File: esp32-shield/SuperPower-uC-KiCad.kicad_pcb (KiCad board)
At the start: 2 copper layers, 45.1 x 45.1 mm, 33 parts, among them J11 DNP, J5 Conn_01x14_Female, J6 Conn_01x14_Female, J9 MCU board, Q3 S8050, Q4 S8050, U13 ESP32-WROOM32, U14 W25Q32JVSS, U5 CH340C, U6 AMS1117-3.3, Y1 12MHZ

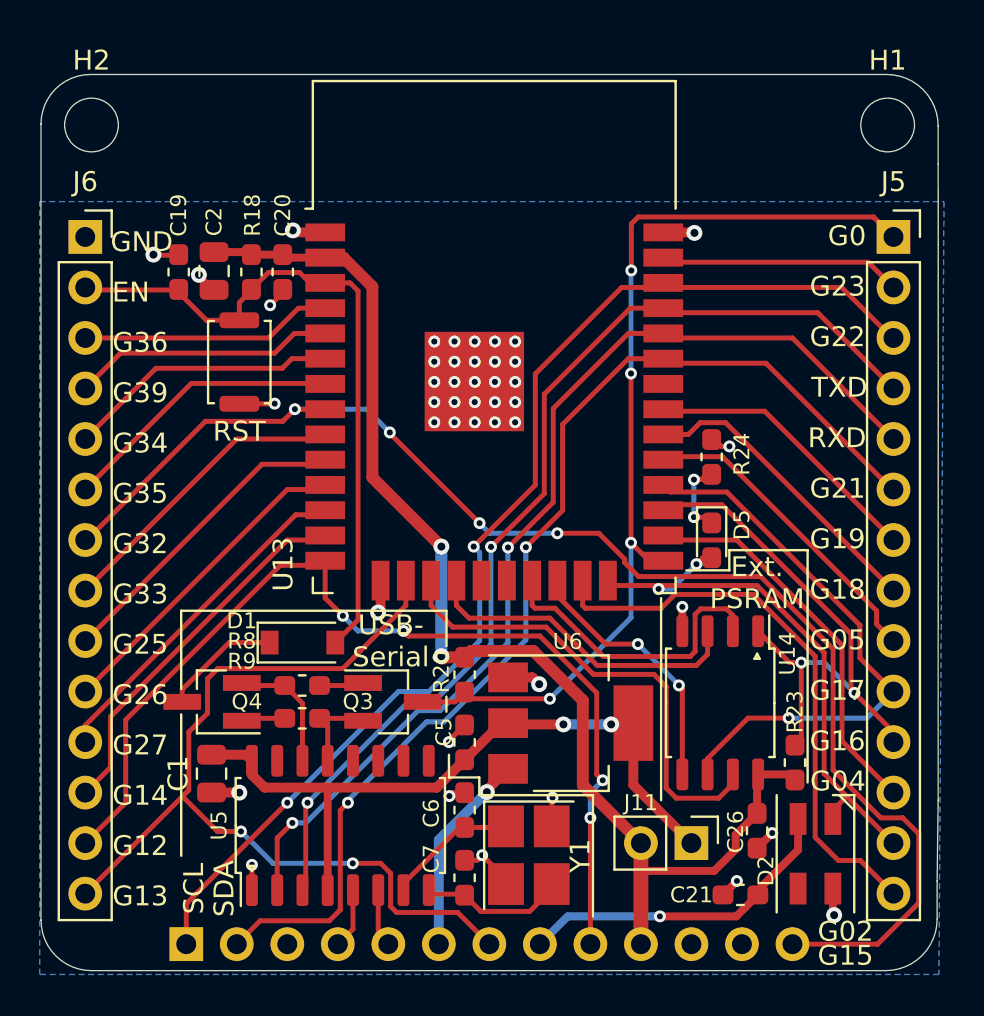
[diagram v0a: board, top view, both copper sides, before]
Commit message: swapped led for WS2812 footprint with logic level shifter
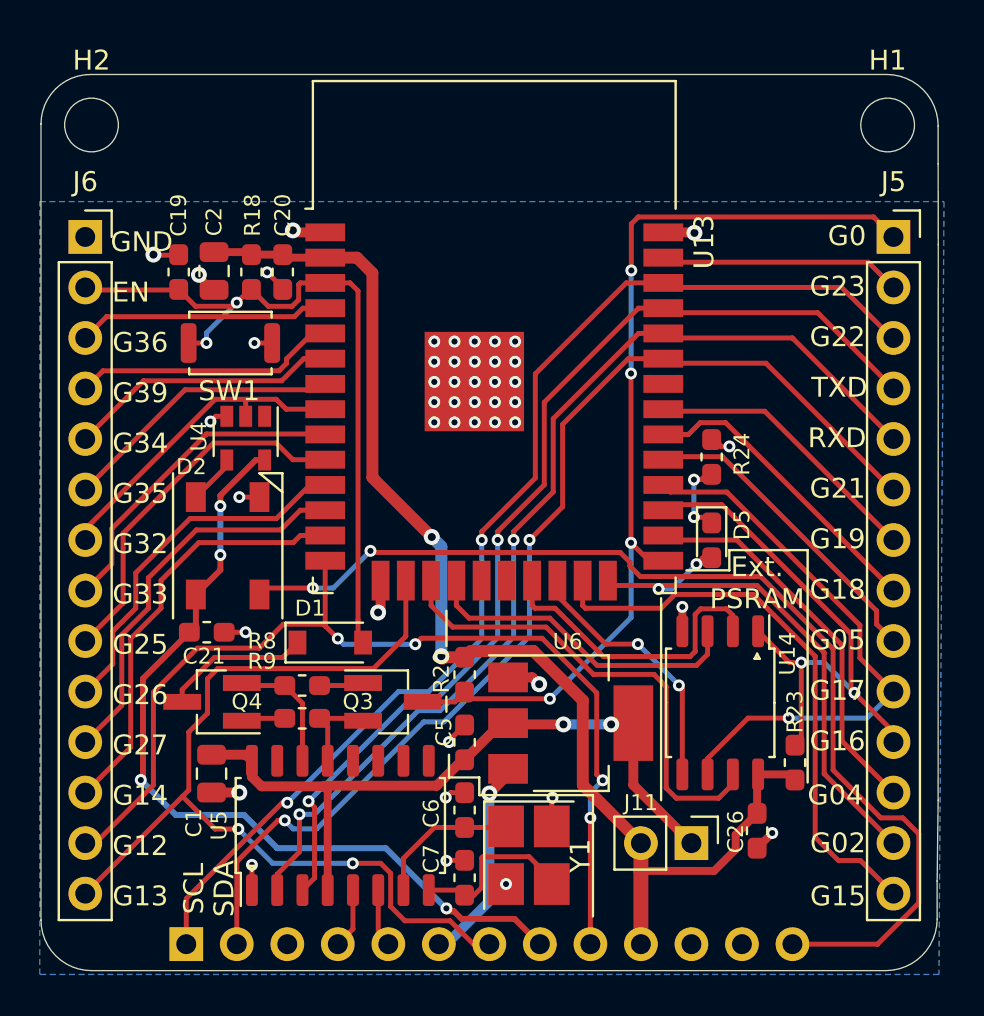
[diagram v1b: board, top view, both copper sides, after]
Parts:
- added U4: SN74LV1T34DBV, Package_TO_SOT_SMD:SOT-23-5, F.Cu at (136.2, 91.7)
- D2: value SK6812MINI -> WS2812B; footprint LED_SMD:LED_SK6812MINI_PLCC4_3.5x3.5mm_P1.75mm -> LED_SMD:LED_WS2812B_PLCC4_5.0x5.0mm_P3.2mm
- SW1: renamed from RST; value DNP -> SKRKAEE020
- moved D2 33.4 mm to (135.3, 97.1)
- moved C21 29.9 mm to (134.2, 101.4), turned to 0 degrees
- moved D1 1.40 mm to (140.4, 101.9)
- moved SW1 1.06 mm to (135.4, 86.9), turned to 0 degrees
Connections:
- D2 pad 1: Net-(D2-Pad1) -> /5V
- D2 pad 2: GND -> /LED_DOUT
- D2 pad 3: /MCU Module/IO2 -> GND
- D2 pad 4: /5V -> Net-(D2-Pad4)
- J6 pad 7: /~SMBALERT -> /MCU Module/IO32
- J9 pad 13: /~SMBALERT -> /LED_DOUT
- U13 pad 8: /~SMBALERT -> /MCU Module/IO32
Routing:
- net /~SMBALERT: track 69.4 -> 0.00 mm, vias 4 -> 0
- net /LED_DOUT: track 0.00 -> 54.3 mm, vias 0 -> 2
- net /5V: track 16.6 -> 42.5 mm, vias 1 -> 4
- net /MCU Module/IO32: track 0.00 -> 16.5 mm
- net /MCU Module/IO25: track 15.8 -> 19.3 mm
- net /MCU Module/IO14: track 18.9 -> 21.8 mm
- net /MCU Module/IO27: track 17.4 -> 20.2 mm
- net /MCU Module/RST: track 35.3 -> 38.0 mm, vias 0 -> 2
- net Net-(D2-Pad4): track 0.00 -> 2.51 mm
- net /MCU Module/IO26: track 16.4 -> 18.7 mm
- net /MCU Module/IO33: track 15.3 -> 17.5 mm
- net Net-(C7-Pad1): track 7.35 -> 9.01 mm
- net GND: track 26.5 -> 24.9 mm, vias 44 -> 46
- net /MCU Module/IO2: track 28.7 -> 27.3 mm
- net Net-(D1-Pad1): track 5.99 -> 7.29 mm
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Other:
- board text added: "LED DOUT"
- board text removed: "USB- Serial"
- board text removed: "~SMBALERT"

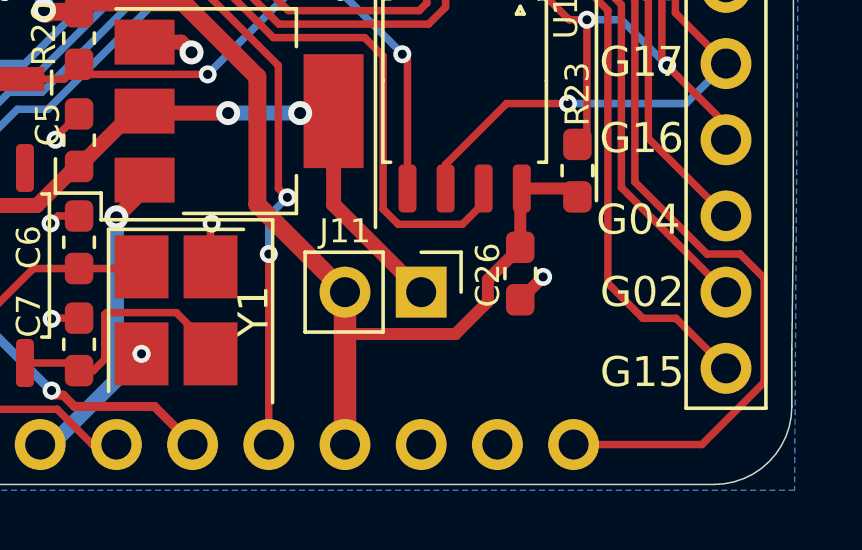
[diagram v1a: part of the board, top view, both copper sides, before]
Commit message: added more silk labels where there was space
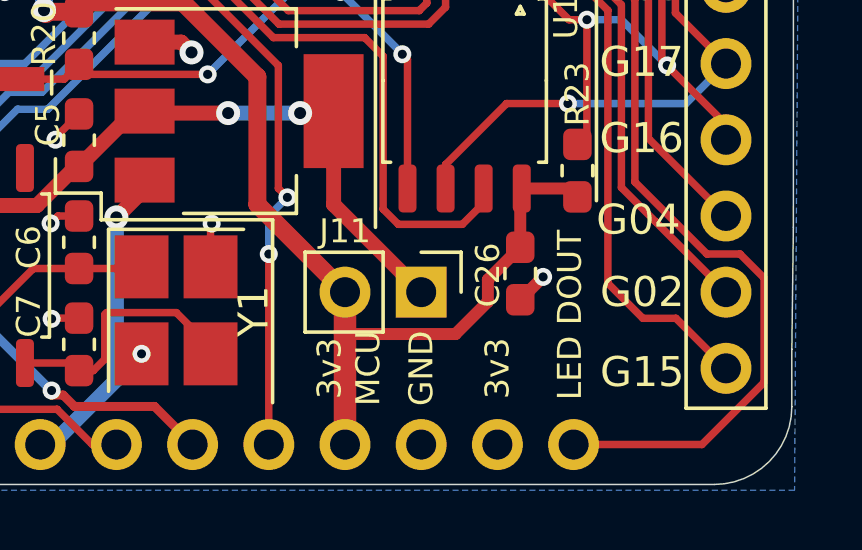
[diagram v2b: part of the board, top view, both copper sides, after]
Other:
- board text added: "3v3 MCU"

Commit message: updated pcb version number and date
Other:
- board text added: "v1.1 (2021-05)"
- board text removed: "v1.00 (2021-02)"

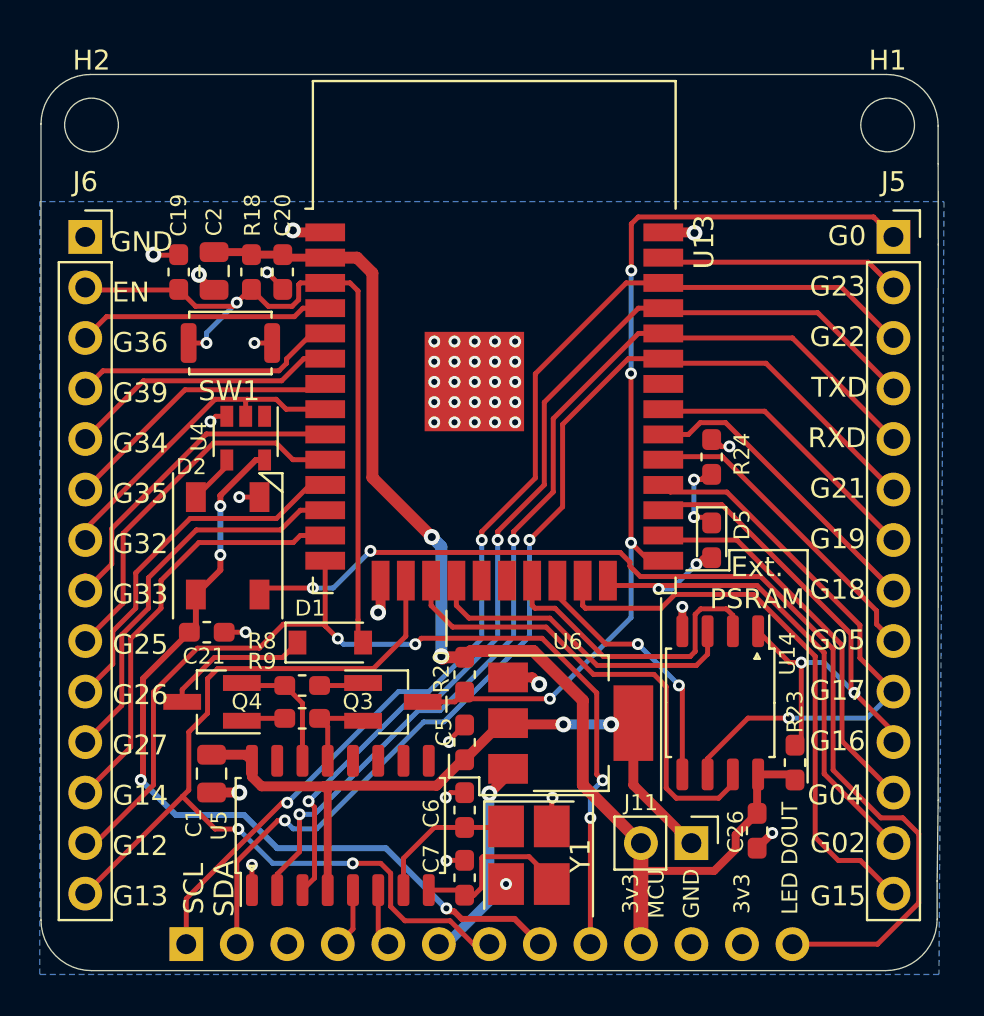
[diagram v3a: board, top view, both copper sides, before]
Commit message: RGB led on right side and using pin 2
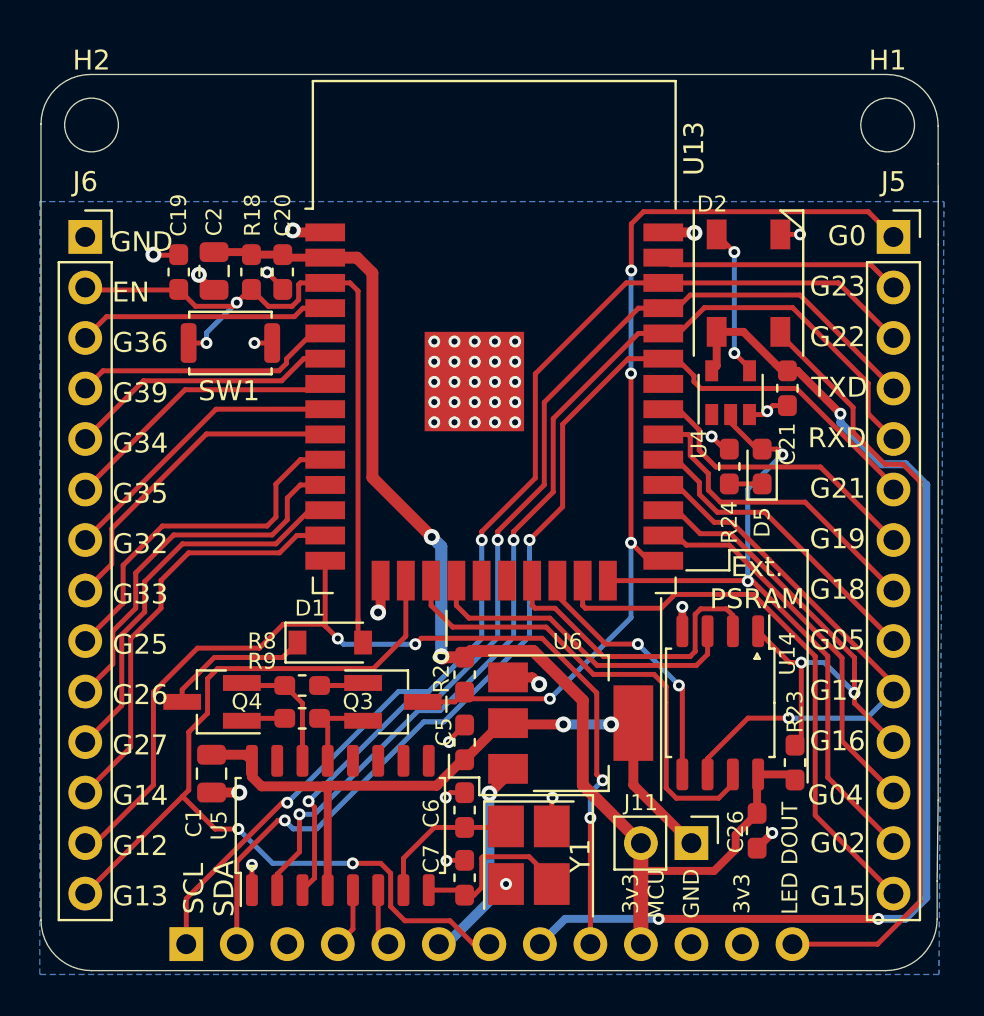
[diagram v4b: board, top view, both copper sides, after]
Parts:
- moved C21 31.7 mm to (163.4, 89.1), turned to 270 degrees
- moved D2 29.3 mm to (161.5, 83.9)
- moved U4 24.5 mm to (160.6, 89.4), turned to 90 degrees
- moved D5 4.50 mm to (162.2, 93.1), turned to 90 degrees
- moved R24 1.01 mm to (160.5, 93.1)
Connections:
- U4 pad 2: /MCU Module/IO32 -> /MCU Module/IO2
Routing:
- net /LED_DOUT: track 54.3 -> 39.4 mm, vias 2 -> 0
- net /5V: track 42.5 -> 57.2 mm, vias 4 -> 3
- net /MCU Module/IO2: track 27.3 -> 34.6 mm
- net Net-(D2-Pad4): track 2.51 -> 7.54 mm, vias 0 -> 2
- net Net-(D5-Pad1): track 3.89 -> 1.65 mm, vias 2 -> 0
- net /MCU Module/RX: track 51.6 -> 53.6 mm
- net /MCU Module/IO18: track 15.3 -> 16.6 mm
- net /MCU Module/IO32: track 16.5 -> 15.4 mm
- net /MCU Module/IO16: track 29.0 -> 28.2 mm
- net /MCU Module/IO17: track 28.4 -> 27.6 mm
- net /MCU Module/IO25: track 19.3 -> 18.7 mm
- net /MCU Module/IO15: track 28.8 -> 28.1 mm
- net /MCU Module/IO26: track 18.7 -> 19.3 mm
- net /MCU Module/IO19: track 14.3 -> 14.9 mm
- net /MCU Module/TX: track 51.8 -> 52.3 mm
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
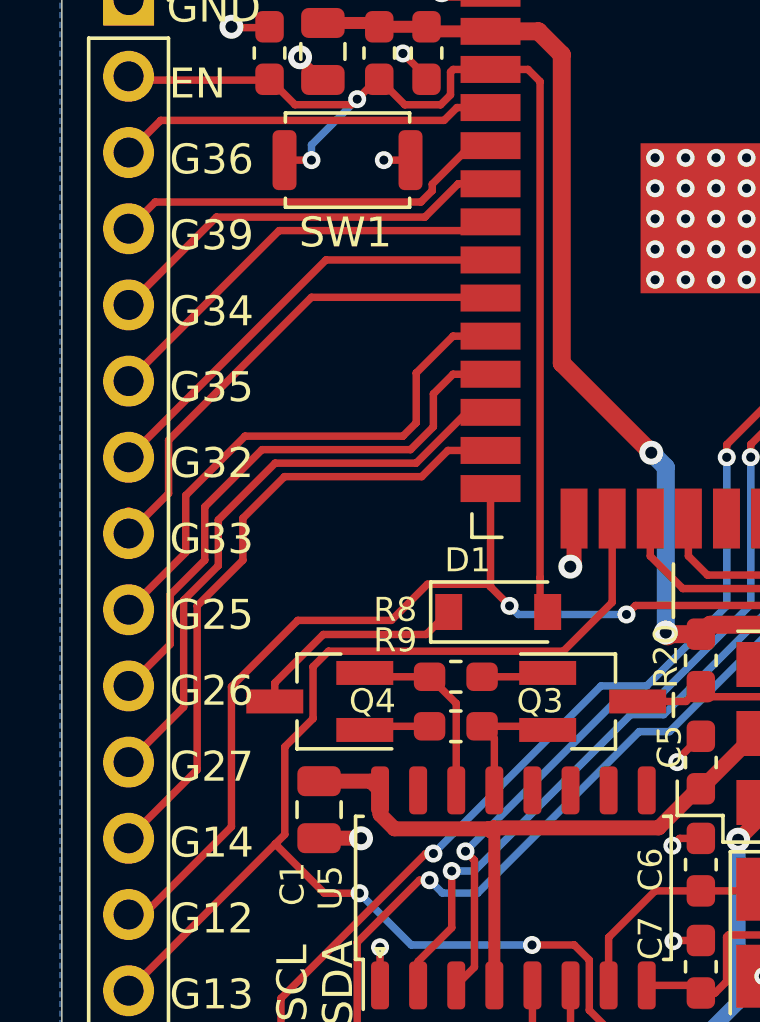
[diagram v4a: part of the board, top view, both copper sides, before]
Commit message: rearranged tracks on left side
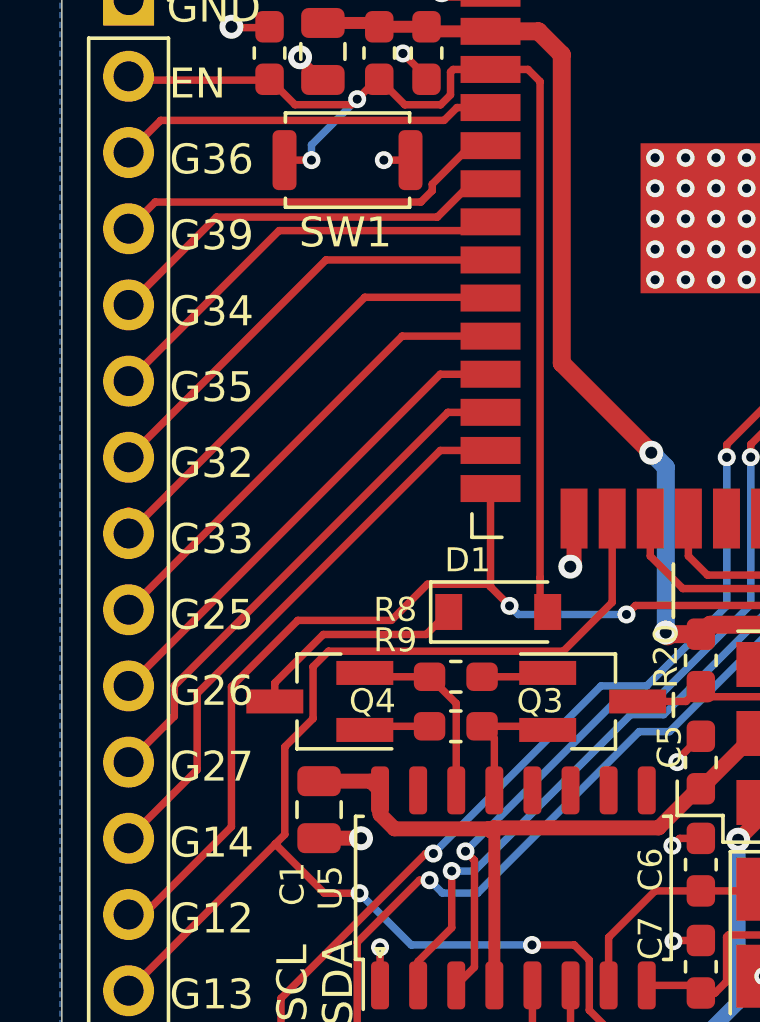
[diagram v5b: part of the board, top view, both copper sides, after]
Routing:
- net /MCU Module/IO26: track 19.3 -> 16.4 mm
- net /MCU Module/IO14: track 21.8 -> 18.9 mm
- net /MCU Module/IO25: track 18.7 -> 15.8 mm
- net /MCU Module/IO27: track 20.2 -> 17.5 mm
- net /MCU Module/IO33: track 17.5 -> 16.4 mm

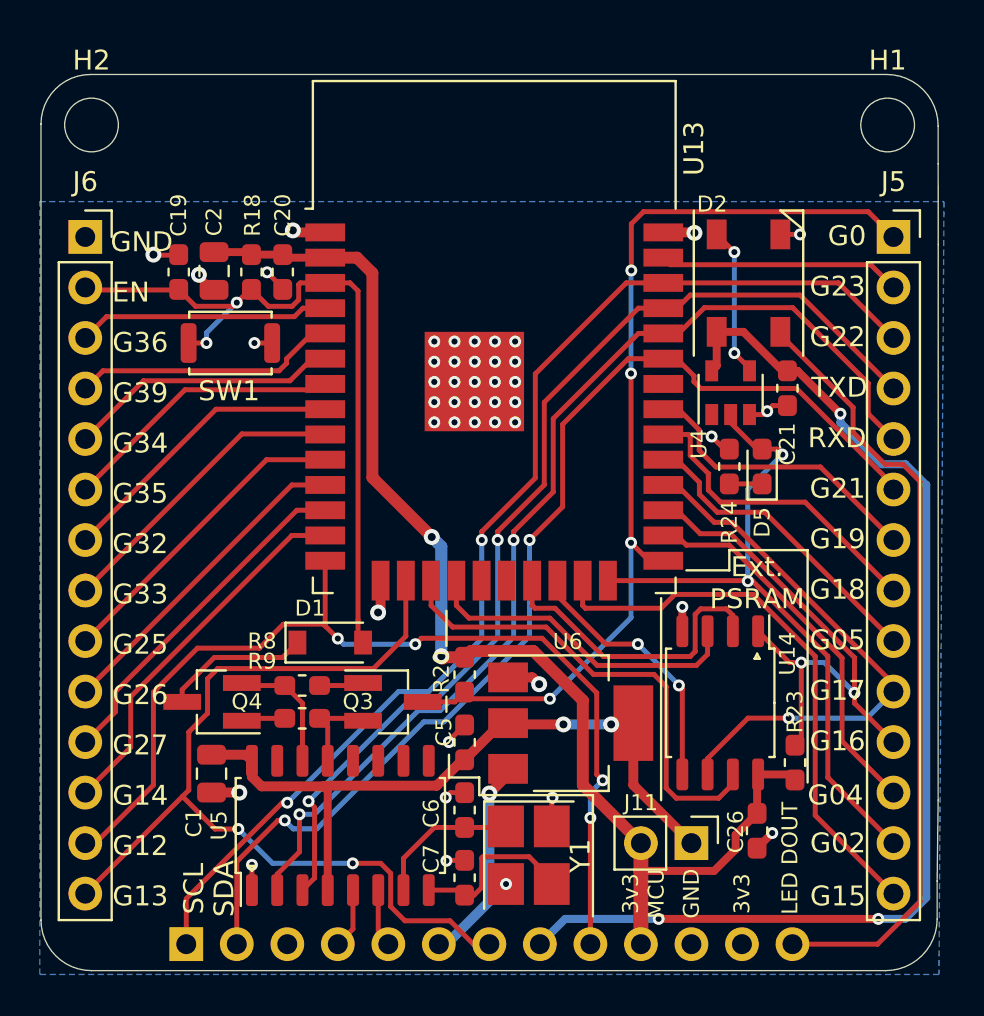
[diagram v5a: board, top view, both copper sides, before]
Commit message: some minor silk and routing improvements
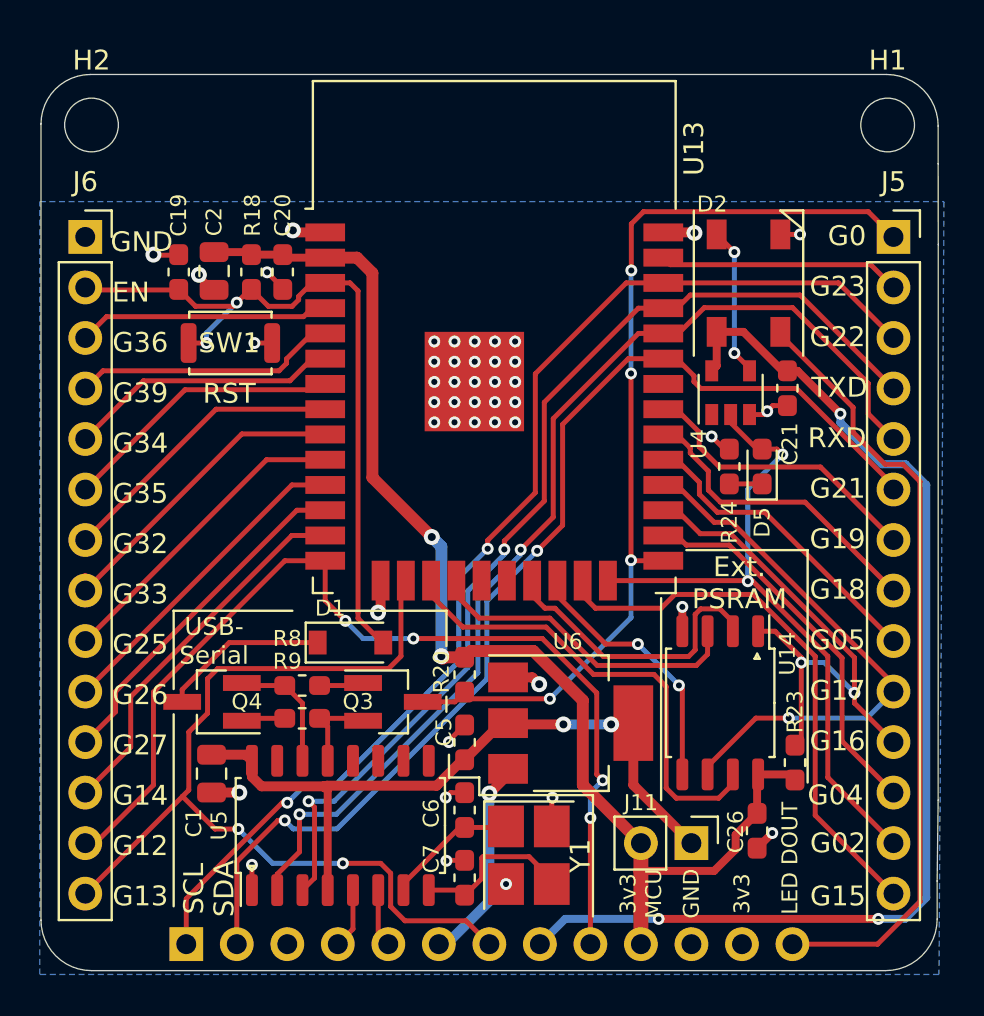
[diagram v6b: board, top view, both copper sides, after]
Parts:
- moved D1 1.02 mm to (141.5, 101.9)
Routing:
- net Net-(D1-Pad1): track 7.29 -> 8.41 mm
- net Net-(C6-Pad1): track 7.52 -> 6.78 mm
- net /EN_3v3: track 52.0 -> 51.3 mm
- net /MCU Module/PSRAM_SD0: track 15.4 -> 14.9 mm
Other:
- board text added: "RST"
- board text added: "USB- Serial"
